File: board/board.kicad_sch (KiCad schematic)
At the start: 95 parts, among them IC1 tps610981dser, IC2 LTR-303ALS-01, IC3 EFM32TG108F32-D-QFN24, IC4 AT30TS74-SS8M-B, IC5 ADA4528-2, IC6 TLV70245_SOT23-5, J1 Conn_01x05_Male, J2 , J3 , J4 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

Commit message: minor
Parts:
- C15, C17, C18, C19, IC5, R17, R18, R19, R20, R21: DNF (none) -> OPTIONAL
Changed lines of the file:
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@@
+      (effects (font (size 1.27 1.27)) hide)
+    )
+    (property "DNF" "OPTIONAL" (id 5) (at 327.66 86.36 90)
       (effects (font (size 1.27 1.27)) hide)
     )
@@
       (effects (font (size 1.27 1.27)) hide)
     )
+    (property "DNF" "OPTIONAL" (id 5) (at 332.74 99.06 90)
+      (effects (font (size 1.27 1.27)) hide)
+    )
   )
   (symbol (lib_name "Device:R_11") (lib_id "Device:R") (at 334.01 80.01 0) (unit 1)
@@
       (effects (font (size 1.27 1.27)) hide)
     )
+    (property "DNF" "OPTIONAL" (id 5) (at 334.01 80.01 90)
+      (effects (font (size 1.27 1.27)) hide)
+    )
   )
   (symbol (lib_name "Device:R_3") (lib_id "Device:R") (at 342.9 107.95 0) (unit 1)
@@
       (effects (font (size 1.27 1.27)) hide)
     )
+    (property "DNF" "OPTIONAL" (id 5) (at 342.9 107.95 90)
+      (effects (font (size 1.27 1.27)) hide)
+    )
   )
   (symbol (lib_name "Device:R_4") (lib_id "Device:R") (at 368.3 96.52 90) (unit 1)
@@
       (effects (font (size 1.27 1.27)) hide)
     )
+    (property "DNF" "OPTIONAL" (id 5) (at 368.3 96.52 90)
+      (effects (font (size 1.27 1.27)) hide)
+    )
   )
   (symbol (lib_id "Jumper:SolderJumper_2_Bridged") (at 208.28 21.59 0) (unit 1)
@@
       (effects (font (size 1.27 1.27)) hide)
     )
+    (property "DNF" "OPTIONAL" (id 5) (at 346.71 53.34 0)
+      (effects (font (size 1.27 1.27)) hide)
+    )
   )
   (symbol (lib_name "pspice:CAP_1") (lib_id "pspice:CAP") (at 368.3 111.76 270) (unit 1)
@@
       (effects (font (size 1.27 1.27)) hide)
     )
-  )
-  (symbol (lib_id "pspice:CAP") (at 374.65 30.48 180) (unit 1)
+    (property "DNF" "OPTIONAL" (id 5) (at 368.3 111.76 0)
+      (effects (font (size 1.27 1.27)) hide)
+    )
+  )
+  (symbol (lib_name "pspice:CAP_6") (lib_id "pspice:CAP") (at 374.65 30.48 180) (unit 1)
     (property "Reference" "C19" (id 0) (at 379.1712 29.3116 0)
       (effects (font (size 1.27 1.27)) (justify right))
@@
       (effects (font (size 1.27 1.27)) hide)
     )
-  )
-  (symbol (lib_id "pspice:CAP") (at 401.32 55.88 0) (unit 1)
+    (property "DNF" "OPTIONAL" (id 5) (at 374.65 30.48 0)
+      (effects (font (size 1.27 1.27)) hide)
+    )
+  )
+  (symbol (lib_name "pspice:CAP_5") (lib_id "pspice:CAP") (at 401.32 55.88 0) (unit 1)
     (property "Reference" "C18" (id 0) (at 393.319 55.88 90))
     (property "Value" "1u" (id 1) (at 395.6304 55.88 90))
@@
     )
     (property "MPN" "CL10B105KP8NNNC" (id 4) (at 401.32 55.88 90)
+      (effects (font (size 1.27 1.27)) hide)
+    )
+    (property "DNF" "OPTIONAL" (id 5) (at 401.32 55.88 90)
       (effects (font (size 1.27 1.27)) hide)
     )
@@
       (effects (font (size 1.27 1.27)) hide)
     )
+    (property "DNF" "OPTIONAL" (id 5) (at 353.06 91.44 0)
+      (effects (font (size 1.27 1.27)) hide)
+    )

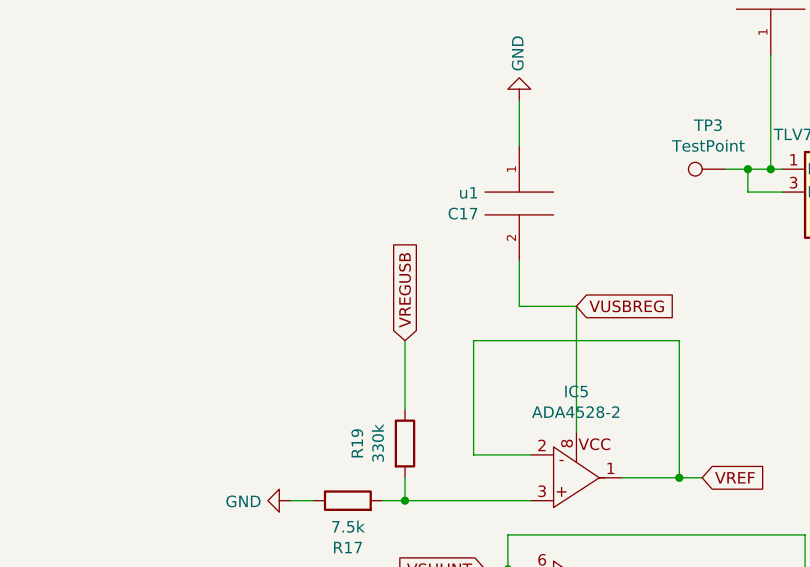
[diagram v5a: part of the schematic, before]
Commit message: fix stupid circuit bug
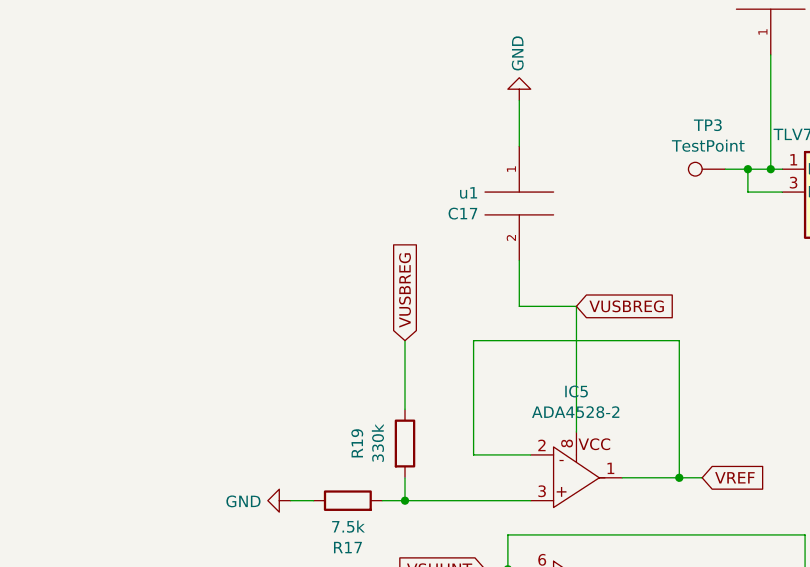
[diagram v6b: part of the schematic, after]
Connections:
- net VREGUSB is gone; now on net VUSBREG: R19.1
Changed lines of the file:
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@@
 (kicad_sch (version 20200506) (host eeschema "(5.99.0-1555-g464399a0c)")
   (page "A0")
+  (junction (at 69.85 166.37))
   (junction (at 342.9 99.06))
+  (junction (at 48.26 50.8))
+  (junction (at 35.56 76.2))
+  (junction (at 200.66 31.75))
+  (junction (at 219.71 93.98))
+  (junction (at 60.96 50.8))
+  (junction (at 69.85 78.74))
+  (junction (at 69.85 27.94))
+  (junction (at 35.56 38.1))
+  (junction (at 237.49 104.14))
+  (junction (at 73.66 63.5))
+  (junction (at 372.11 49.53))
+  (junction (at 213.36 21.59))
+  (junction (at 44.45 27.94))
+  (junction (at 48.26 88.9))
+  (junction (at 200.66 43.18))
+  (junction (at 60.96 38.1))
+  (junction (at 203.2 31.75))
+  (junction (at 57.15 40.64))
+  (junction (at 44.45 40.64))
+  (junction (at 73.66 76.2))
+  (junction (at 73.66 88.9))
+  (junction (at 99.06 76.2))
+  (junction (at 69.85 50.8))
+  (junction (at 31.75 88.9))
+  (junction (at 139.7 93.98))
+  (junction (at 187.96 53.34))
+  (junction (at 44.45 53.34))
+  (junction (at 116.84 99.06))
+  (junction (at 48.26 63.5))
+  (junction (at 35.56 50.8))
+  (junction (at 374.65 49.53))
+  (junction (at 95.25 78.74))
+  (junction (at 345.44 93.98))
+  (junction (at 35.56 63.5))
+  (junction (at 342.9 114.3))
+  (junction (at 31.75 40.64))
+  (junction (at 73.66 25.4))
+  (junction (at 31.75 66.04))
+  (junction (at 31.75 27.94))
+  (junction (at 360.68 111.76))
+  (junction (at 57.15 78.74))
+  (junction (at 57.15 66.04))
+  (junction (at 82.55 66.04))
   (junction (at 60.96 76.2))
-  (junction (at 48.26 88.9))
+  (junction (at 82.55 40.64))
+  (junction (at 73.66 38.1))
+  (junction (at 93.98 123.19))
+  (junction (at 31.75 53.34))
+  (junction (at 378.46 96.52))
+  (junction (at 82.55 38.1))
+  (junction (at 69.85 53.34))
+  (junction (at 93.98 119.38))
+  (junction (at 334.01 86.36))
+  (junction (at 116.84 153.67))
+  (junction (at 48.26 25.4))
+  (junction (at 86.36 50.8))
+  (junction (at 213.36 31.75))
+  (junction (at 44.45 78.74))
+  (junction (at 360.68 96.52))
+  (junction (at 95.25 25.4))
+  (junction (at 60.96 88.9))
+  (junction (at 123.19 93.98))
+  (junction (at 60.96 25.4))
+  (junction (at 129.54 102.87))
+  (junction (at 99.06 88.9))
+  (junction (at 401.32 49.53))
+  (junction (at 251.46 104.14))
+  (junction (at 86.36 25.4))
+  (junction (at 53.34 167.64))
+  (junction (at 24.13 143.51))
+  (junction (at 82.55 53.34))
+  (junction (at 95.25 66.04))
+  (junction (at 44.45 76.2))
+  (junction (at 187.96 154.94))
+  (junction (at 203.2 154.94))
   (junction (at 48.26 38.1))
-  (junction (at 82.55 53.34))
-  (junction (at 69.85 27.94))
-  (junction (at 35.56 25.4))
-  (junction (at 35.56 76.2))
-  (junction (at 82.55 66.04))
-  (junction (at 82.55 148.59))
-  (junction (at 95.25 78.74))
+  (junction (at 57.15 27.94))
+  (junction (at 86.36 63.5))
+  (junction (at 86.36 76.2))
   (junction (at 24.13 167.64))
-  (junction (at 44.45 27.94))
-  (junction (at 60.96 25.4))
-  (junction (at 187.96 53.34))
-  (junction (at 69.85 50.8))
-  (junction (at 86.36 50.8))
-  (junction (at 93.98 123.19))
-  (junction (at 116.84 99.06))
-  (junction (at 378.46 96.52))
-  (junction (at 69.85 78.74))
-  (junction (at 401.32 49.53))
-  (junction (at 44.45 53.34))
-  (junction (at 44.45 40.64))
-  (junction (at 35.56 38.1))
-  (junction (at 73.66 76.2))
+  (junction (at 38.1 185.42))
   (junction (at 364.49 83.82))
-  (junction (at 374.65 49.53))
-  (junction (at 203.2 31.75))
-  (junction (at 35.56 63.5))
-  (junction (at 116.84 153.67))
-  (junction (at 82.55 38.1))
-  (junction (at 60.96 88.9))
-  (junction (at 60.96 50.8))
-  (junction (at 95.25 25.4))
-  (junction (at 31.75 66.04))
-  (junction (at 139.7 93.98))
-  (junction (at 237.49 104.14))
-  (junction (at 219.71 93.98))
-  (junction (at 57.15 27.94))
-  (junction (at 57.15 40.64))
-  (junction (at 372.11 49.53))
-  (junction (at 203.2 154.94))
-  (junction (at 360.68 111.76))
-  (junction (at 38.1 185.42))
-  (junction (at 95.25 66.04))
-  (junction (at 200.66 31.75))
-  (junction (at 38.1 167.64))
-  (junction (at 123.19 93.98))
-  (junction (at 73.66 25.4))
   (junction (at 69.85 66.04))
   (junction (at 203.2 140.97))
-  (junction (at 31.75 88.9))
-  (junction (at 73.66 88.9))
-  (junction (at 73.66 63.5))
-  (junction (at 31.75 40.64))
-  (junction (at 334.01 86.36))
-  (junction (at 86.36 63.5))
-  (junction (at 360.68 96.52))
-  (junction (at 48.26 50.8))
-  (junction (at 31.75 27.94))
-  (junction (at 342.9 114.3))
-  (junction (at 31.75 53.34))
-  (junction (at 48.26 25.4))
-  (junction (at 200.66 43.18))
+  (junction (at 82.55 148.59))
+  (junction (at 35.56 25.4))
   (junction (at 57.15 63.5))
-  (junction (at 213.36 21.59))
-  (junction (at 69.85 53.34))
-  (junction (at 82.55 40.64))
-  (junction (at 60.96 38.1))
-  (junction (at 73.66 38.1))
-  (junction (at 24.13 143.51))
-  (junction (at 99.06 76.2))
-  (junction (at 57.15 66.04))
-  (junction (at 69.85 166.37))
-  (junction (at 187.96 154.94))
-  (junction (at 57.15 78.74))
-  (junction (at 129.54 102.87))
-  (junction (at 35.56 50.8))
-  (junction (at 86.36 25.4))
-  (junction (at 99.06 88.9))
-  (junction (at 44.45 78.74))
-  (junction (at 213.36 31.75))
-  (junction (at 53.34 167.64))
-  (junction (at 345.44 93.98))
-  (junction (at 251.46 104.14))
-  (junction (at 48.26 63.5))
-  (junction (at 86.36 76.2))
-  (junction (at 93.98 119.38))
-  (junction (at 44.45 76.2))
-  (no_connect (at 72.39 119.38))
+  (junction (at 38.1 167.64))
   (no_connect (at 198.12 129.54))
   (no_connect (at 41.91 227.33))
+  (no_connect (at 27.94 217.17))
+  (no_connect (at 72.39 119.38))
   (no_connect (at 41.91 217.17))
+  (no_connect (at 138.43 158.75))
   (no_connect (at 193.04 129.54))
   (no_connect (at 35.56 234.95))
-  (no_connect (at 27.94 217.17))
-  (no_connect (at 138.43 158.75))
   (no_connect (at 27.94 227.33))
   (wire (pts (xy 19.05 167.64) (xy 24.13 167.64)))
@@
     (effects (font (size 1.27 1.27)) (justify right))
   )
-  (global_label "VREGUSB" (shape input) (at 334.01 68.58 90)
-    (effects (font (size 1.27 1.27)) (justify left))
-  )
+  (global_label "VUSBREG" (shape input) (at 334.01 68.58 90)
+    (effects (font (size 1.27 1.27)) (justify left))
+  )

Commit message: add wire pad for vshunt
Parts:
- added TP6: TestPoint, TestPoint:TestPoint_Pad_3.0x3.0mm, symbol Connector:TestPoint
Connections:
- net VSHUNT: now also TP6.1
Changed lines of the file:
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@@
   (junction (at 60.96 50.8))
   (junction (at 69.85 78.74))
+  (junction (at 219.71 21.59))
   (junction (at 69.85 27.94))
   (junction (at 35.56 38.1))
@@
   (wire (pts (xy 218.44 109.22) (xy 220.98 109.22)))
   (wire (pts (xy 218.44 114.3) (xy 220.98 114.3)))
+  (wire (pts (xy 219.71 10.16) (xy 219.71 21.59)))
+  (wire (pts (xy 219.71 21.59) (xy 213.36 21.59)))
   (wire (pts (xy 219.71 43.18) (xy 200.66 43.18)))
   (wire (pts (xy 219.71 43.18) (xy 219.71 39.37)))
@@
   (wire (pts (xy 220.98 140.97) (xy 226.06 140.97)))
   (wire (pts (xy 220.98 154.94) (xy 226.06 154.94)))
-  (wire (pts (xy 223.52 21.59) (xy 213.36 21.59)))
+  (wire (pts (xy 223.52 21.59) (xy 219.71 21.59)))
   (wire (pts (xy 224.79 31.75) (xy 234.95 31.75)))
   (wire (pts (xy 228.6 109.22) (xy 229.87 109.22)))
@@
     )
     (property "Datasheet" "~" (id 3) (at 158.75 27.94 0)
+      (effects (font (size 1.27 1.27)) hide)
+    )
+  )
+  (symbol (lib_name "Connector:TestPoint_4") (lib_id "Connector:TestPoint") (at 219.71 10.16 0) (unit 1)
+    (property "Reference" "TP6" (id 0) (at 224.5552 8.3185 90))
+    (property "Value" "TestPoint" (id 1) (at 222.2565 8.3185 90))
+    (property "Footprint" "TestPoint:TestPoint_Pad_3.0x3.0mm" (id 2) (at 224.79 10.16 0)
+      (effects (font (size 1.27 1.27)) hide)
+    )
+    (property "Datasheet" "~" (id 3) (at 224.79 10.16 0)
       (effects (font (size 1.27 1.27)) hide)
     )
@@
     (path "/f91953b6-2fde-4116-bbe0-522f3605ce9d" (reference "TP4") (unit 1))
     (path "/7d5cf4f0-2156-472a-933d-95df0ad9b0db" (reference "TP5") (unit 1))
+    (path "/9ae8e418-62ff-40a3-ace6-bc35702411d4" (reference "TP6") (unit 1))
   )
 )

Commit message: correct mpns for 23.2 ohm resistors
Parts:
- R10, R3, R4, R5, R6, R9: MPN ERJ-2RKF23R2X -> ERJ-3EKF23R2V
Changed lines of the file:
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@@
 (kicad_sch (version 20200506) (host eeschema "(5.99.0-1555-g464399a0c)")
   (page "A0")
-  (junction (at 69.85 166.37))
+  (junction (at 38.1 185.42))
+  (junction (at 35.56 63.5))
+  (junction (at 35.56 25.4))
+  (junction (at 93.98 123.19))
+  (junction (at 187.96 154.94))
+  (junction (at 44.45 76.2))
+  (junction (at 99.06 88.9))
+  (junction (at 73.66 88.9))
+  (junction (at 69.85 78.74))
+  (junction (at 60.96 38.1))
+  (junction (at 60.96 25.4))
+  (junction (at 53.34 167.64))
+  (junction (at 86.36 76.2))
   (junction (at 342.9 99.06))
-  (junction (at 48.26 50.8))
-  (junction (at 35.56 76.2))
-  (junction (at 200.66 31.75))
+  (junction (at 345.44 93.98))
+  (junction (at 378.46 96.52))
+  (junction (at 69.85 50.8))
+  (junction (at 73.66 76.2))
+  (junction (at 69.85 53.34))
+  (junction (at 200.66 43.18))
+  (junction (at 95.25 66.04))
+  (junction (at 35.56 38.1))
+  (junction (at 38.1 167.64))
+  (junction (at 57.15 63.5))
+  (junction (at 57.15 40.64))
+  (junction (at 48.26 38.1))
+  (junction (at 60.96 76.2))
+  (junction (at 364.49 83.82))
+  (junction (at 31.75 27.94))
+  (junction (at 129.54 102.87))
+  (junction (at 203.2 140.97))
+  (junction (at 73.66 63.5))
+  (junction (at 31.75 53.34))
+  (junction (at 48.26 88.9))
   (junction (at 219.71 93.98))
   (junction (at 60.96 50.8))
-  (junction (at 69.85 78.74))
-  (junction (at 219.71 21.59))
-  (junction (at 69.85 27.94))
-  (junction (at 35.56 38.1))
-  (junction (at 237.49 104.14))
-  (junction (at 73.66 63.5))
-  (junction (at 372.11 49.53))
-  (junction (at 213.36 21.59))
-  (junction (at 44.45 27.94))
-  (junction (at 48.26 88.9))
-  (junction (at 200.66 43.18))
-  (junction (at 60.96 38.1))
-  (junction (at 203.2 31.75))
-  (junction (at 57.15 40.64))
-  (junction (at 44.45 40.64))
-  (junction (at 73.66 76.2))
-  (junction (at 73.66 88.9))
-  (junction (at 99.06 76.2))
-  (junction (at 69.85 50.8))
-  (junction (at 31.75 88.9))
-  (junction (at 139.7 93.98))
-  (junction (at 187.96 53.34))
-  (junction (at 44.45 53.34))
+  (junction (at 35.56 76.2))
+  (junction (at 82.55 40.64))
+  (junction (at 69.85 66.04))
   (junction (at 116.84 99.06))
-  (junction (at 48.26 63.5))
-  (junction (at 35.56 50.8))
   (junction (at 374.65 49.53))
-  (junction (at 95.25 78.74))
-  (junction (at 345.44 93.98))
-  (junction (at 35.56 63.5))
-  (junction (at 342.9 114.3))
-  (junction (at 31.75 40.64))
-  (junction (at 73.66 25.4))
-  (junction (at 31.75 66.04))
-  (junction (at 31.75 27.94))
-  (junction (at 360.68 111.76))
-  (junction (at 57.15 78.74))
-  (junction (at 57.15 66.04))
-  (junction (at 82.55 66.04))
-  (junction (at 60.96 76.2))
-  (junction (at 82.55 40.64))
-  (junction (at 73.66 38.1))
-  (junction (at 93.98 123.19))
-  (junction (at 31.75 53.34))
-  (junction (at 378.46 96.52))
-  (junction (at 82.55 38.1))
-  (junction (at 69.85 53.34))
-  (junction (at 93.98 119.38))
-  (junction (at 334.01 86.36))
+  (junction (at 82.55 148.59))
   (junction (at 116.84 153.67))
   (junction (at 48.26 25.4))
+  (junction (at 73.66 38.1))
+  (junction (at 82.55 38.1))
+  (junction (at 69.85 166.37))
+  (junction (at 237.49 104.14))
+  (junction (at 123.19 93.98))
+  (junction (at 48.26 50.8))
+  (junction (at 73.66 25.4))
+  (junction (at 342.9 114.3))
+  (junction (at 60.96 88.9))
+  (junction (at 334.01 86.36))
+  (junction (at 203.2 154.94))
+  (junction (at 95.25 78.74))
+  (junction (at 200.66 31.75))
+  (junction (at 24.13 167.64))
+  (junction (at 213.36 31.75))
+  (junction (at 57.15 78.74))
+  (junction (at 82.55 53.34))
+  (junction (at 24.13 143.51))
+  (junction (at 187.96 53.34))
+  (junction (at 82.55 66.04))
+  (junction (at 86.36 63.5))
+  (junction (at 99.06 76.2))
+  (junction (at 95.25 25.4))
+  (junction (at 401.32 49.53))
+  (junction (at 44.45 27.94))
+  (junction (at 203.2 31.75))
+  (junction (at 251.46 104.14))
+  (junction (at 44.45 78.74))
+  (junction (at 35.56 50.8))
+  (junction (at 31.75 40.64))
+  (junction (at 57.15 66.04))
+  (junction (at 31.75 66.04))
+  (junction (at 213.36 21.59))
+  (junction (at 86.36 25.4))
+  (junction (at 57.15 27.94))
+  (junction (at 372.11 49.53))
   (junction (at 86.36 50.8))
-  (junction (at 213.36 31.75))
-  (junction (at 44.45 78.74))
   (junction (at 360.68 96.52))
-  (junction (at 95.25 25.4))
-  (junction (at 60.96 88.9))
-  (junction (at 123.19 93.98))
-  (junction (at 60.96 25.4))
-  (junction (at 129.54 102.87))
-  (junction (at 99.06 88.9))
-  (junction (at 401.32 49.53))
-  (junction (at 251.46 104.14))
-  (junction (at 86.36 25.4))
-  (junction (at 53.34 167.64))
-  (junction (at 24.13 143.51))
-  (junction (at 82.55 53.34))
-  (junction (at 95.25 66.04))
-  (junction (at 44.45 76.2))
-  (junction (at 187.96 154.94))
-  (junction (at 203.2 154.94))
-  (junction (at 48.26 38.1))
-  (junction (at 57.15 27.94))
-  (junction (at 86.36 63.5))
-  (junction (at 86.36 76.2))
-  (junction (at 24.13 167.64))
-  (junction (at 38.1 185.42))
-  (junction (at 364.49 83.82))
-  (junction (at 69.85 66.04))
-  (junction (at 203.2 140.97))
-  (junction (at 82.55 148.59))
-  (junction (at 35.56 25.4))
-  (junction (at 57.15 63.5))
-  (junction (at 38.1 167.64))
+  (junction (at 93.98 119.38))
+  (junction (at 139.7 93.98))
+  (junction (at 44.45 53.34))
+  (junction (at 31.75 88.9))
+  (junction (at 360.68 111.76))
+  (junction (at 219.71 21.59))
+  (junction (at 44.45 40.64))
+  (junction (at 69.85 27.94))
+  (junction (at 48.26 63.5))
   (no_connect (at 198.12 129.54))
+  (no_connect (at 72.39 119.38))
+  (no_connect (at 27.94 217.17))
+  (no_connect (at 193.04 129.54))
+  (no_connect (at 41.91 217.17))
+  (no_connect (at 27.94 227.33))
   (no_connect (at 41.91 227.33))
-  (no_connect (at 27.94 217.17))
-  (no_connect (at 72.39 119.38))
-  (no_connect (at 41.91 217.17))
   (no_connect (at 138.43 158.75))
-  (no_connect (at 193.04 129.54))
   (no_connect (at 35.56 234.95))
-  (no_connect (at 27.94 227.33))
   (wire (pts (xy 19.05 167.64) (xy 24.13 167.64)))
   (wire (pts (xy 24.13 128.27) (xy 24.13 125.73)))
@@
       (effects (font (size 1.27 1.27)) hide)
     )
-    (property "MPN" "ERJ-2RKF23R2X" (id 4) (at 109.22 -104.14 0)
+    (property "MPN" "ERJ-3EKF23R2V" (id 4) (at 109.22 -104.14 0)
       (effects (font (size 1.27 1.27)) hide)
     )
@@
       (effects (font (size 1.27 1.27)) hide)
     )
-    (property "MPN" "ERJ-2RKF23R2X" (id 4) (at 109.22 -99.06 0)
+    (property "MPN" "ERJ-3EKF23R2V" (id 4) (at 109.22 -99.06 0)
       (effects (font (size 1.27 1.27)) hide)
     )
@@
       (effects (font (size 1.27 1.27)) hide)
     )
-    (property "MPN" "ERJ-2RKF23R2X" (id 4) (at -57.15 125.73 0)
+    (property "MPN" "ERJ-3EKF23R2V" (id 4) (at -57.15 125.73 0)
       (effects (font (size 1.27 1.27)) hide)
     )
@@
       (effects (font (size 1.27 1.27)) hide)
     )
-    (property "MPN" "ERJ-2RKF23R2X" (id 4) (at 396.24 91.44 0)
+    (property "MPN" "ERJ-3EKF23R2V" (id 4) (at 396.24 91.44 0)
       (effects (font (size 1.27 1.27)) hide)
     )
@@
       (effects (font (size 1.27 1.27)) hide)
     )
-    (property "MPN" "ERJ-2RKF23R2X" (id 4) (at 180.34 -104.14 0)
+    (property "MPN" "ERJ-3EKF23R2V" (id 4) (at 180.34 -104.14 0)
       (effects (font (size 1.27 1.27)) hide)
     )
@@
       (effects (font (size 1.27 1.27)) hide)
     )
-    (property "MPN" "ERJ-2RKF23R2X" (id 4) (at 180.34 -99.06 0)
-      (effects (font (size 1.27 1.27)) hide)
-    )
+    (property "MPN" "ERJ-3EKF23R2V" (id 4) (at 180.34 -99.06 0)
+      (effects (font (size 1.27 1.27)) hide)
+    )
